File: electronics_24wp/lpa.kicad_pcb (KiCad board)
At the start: 2 copper layers, 143 x 74 mm, 85 parts, among them CON1 BARREL_JACK, IC1 ATMEGA328-A, P2 CONN_3X2, U1 SD_CARD, U2 AP1509, U3 TLC5941, U4 TLC5941, U5 TLC5941, X1 CRYSTAL_SMD

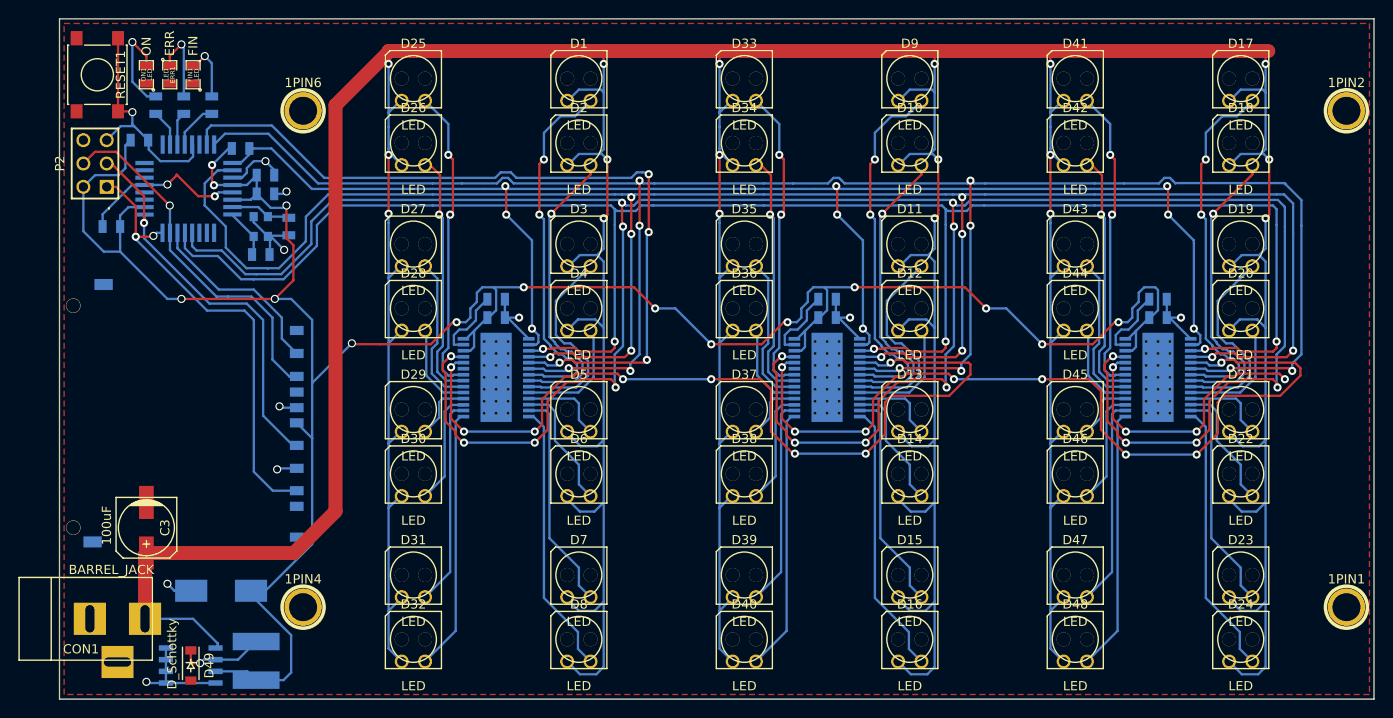
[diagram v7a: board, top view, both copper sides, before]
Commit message: Added VIN plane to PCB layout.
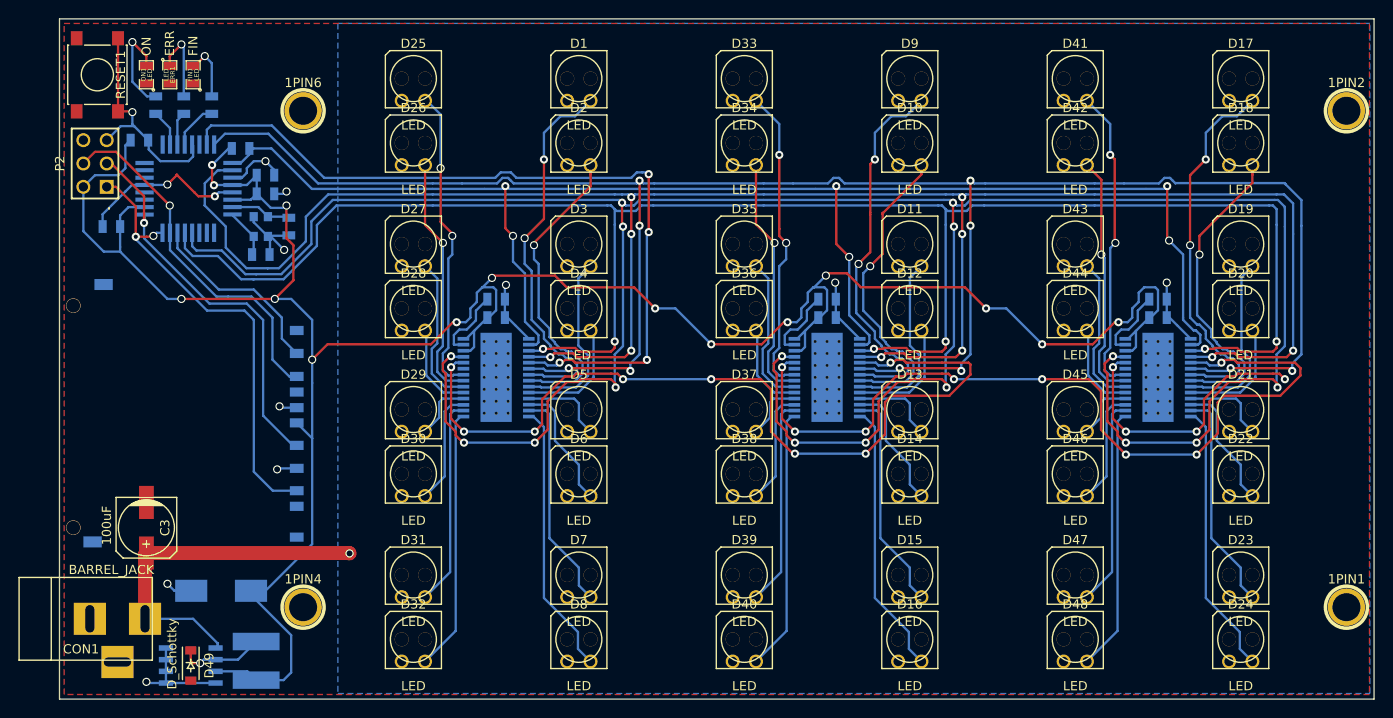
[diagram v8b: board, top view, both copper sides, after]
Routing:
- net /tlcs_1-3/VIN: track 748.3 -> 39.7 mm, vias 18 -> 1
- net /tlcs_1-3/VCC: track 278.2 -> 281.7 mm
- net Net-(D11-Pad2): track 22.3 -> 19.8 mm
- net Net-(D19-Pad2): track 22.3 -> 19.9 mm
- net Net-(D3-Pad2): track 22.3 -> 19.9 mm
- net Net-(D10-Pad2): track 32.8 -> 34.6 mm
- net Net-(D2-Pad2): track 32.8 -> 34.2 mm
- net Net-(D1-Pad2): track 40.5 -> 41.8 mm
- net Net-(D9-Pad2): track 40.5 -> 41.7 mm
- net Net-(D18-Pad2): track 32.8 -> 34.0 mm
- net Net-(D17-Pad2): track 40.5 -> 41.6 mm
- net GND: track 76.0 -> 76.6 mm
- net /tlcs_1-3/BLANK: track 164.1 -> 164.7 mm, vias 9 -> 6
- added copper zone on B.Cu, net /tlcs_1-3/VIN
